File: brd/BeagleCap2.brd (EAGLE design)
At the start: 152.5 x 152 mm, 33 parts, among them IC2 7805TV, J2 DS18B20, J3 Battery, U1 DHT22, X1 Conn BNC : pH, X2 Conn BNC : Dissolved Oxygen, X3 Conn BNC : Conductivity, X4 Conn BNC : ORP

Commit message: Schematic updated with new PCB
Done by JayMcGee
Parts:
- LED1: device led:LED5MM -> led:SML0805
- R1, R10, R2, R3, R4, R5, R6, R7, R8, R9: device adafruit:0207/10 -> adafruit:R0805
- moved C2 96.6 mm to (-58.5, 76.5)
- moved J4 82.7 mm to (-6.50, 6.00)
- moved R8 76.2 mm to (-16.0, 6.00)
- moved D4 76.0 mm to (-16.0, 9.00)
- moved D3 75.7 mm to (-16.0, 0.50)
- moved R10 64.7 mm to (-16.0, 12.0)
- moved R9 64.0 mm to (-16.0, 3.00)
- moved LED1 61.1 mm to (-7.50, 81.5), turned to 0 degrees
- moved R7 56.0 mm to (-7.50, 79.0)
- moved C1 43.8 mm to (-52.0, 76.5)
- moved IC2 43.5 mm to (-29.1, 80.3)
- moved KK1 43.5 mm to (-29.0, 82.0)
- moved R2 16.0 mm to (-16.9, -6.34)
- moved R4 14.4 mm to (-28.6, -6.34)
- moved R1 14.1 mm to (-14.3, -6.84)
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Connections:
- net 3.3V renamed GNDX
- net N$2: now also LED1.C; no longer LED1.K
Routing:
- net GND: track 0.00 -> 36.8 mm
- net 5V: track 0.00 -> 35.8 mm
- net N$1: track 0.00 -> 15.6 mm
- net VIN: track 0.00 -> 8.85 mm
- added copper zone on layer 16, net GND
- added copper zone on layer 1, net GNDX
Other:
- board size 152.5 x 152 mm -> 75.5 x 152 mm
- board text added: "AQUARIUS"
- board text added: "Jean-Philippe Fournier Jean-Pascal McGee"
- board text removed: "SIM908"

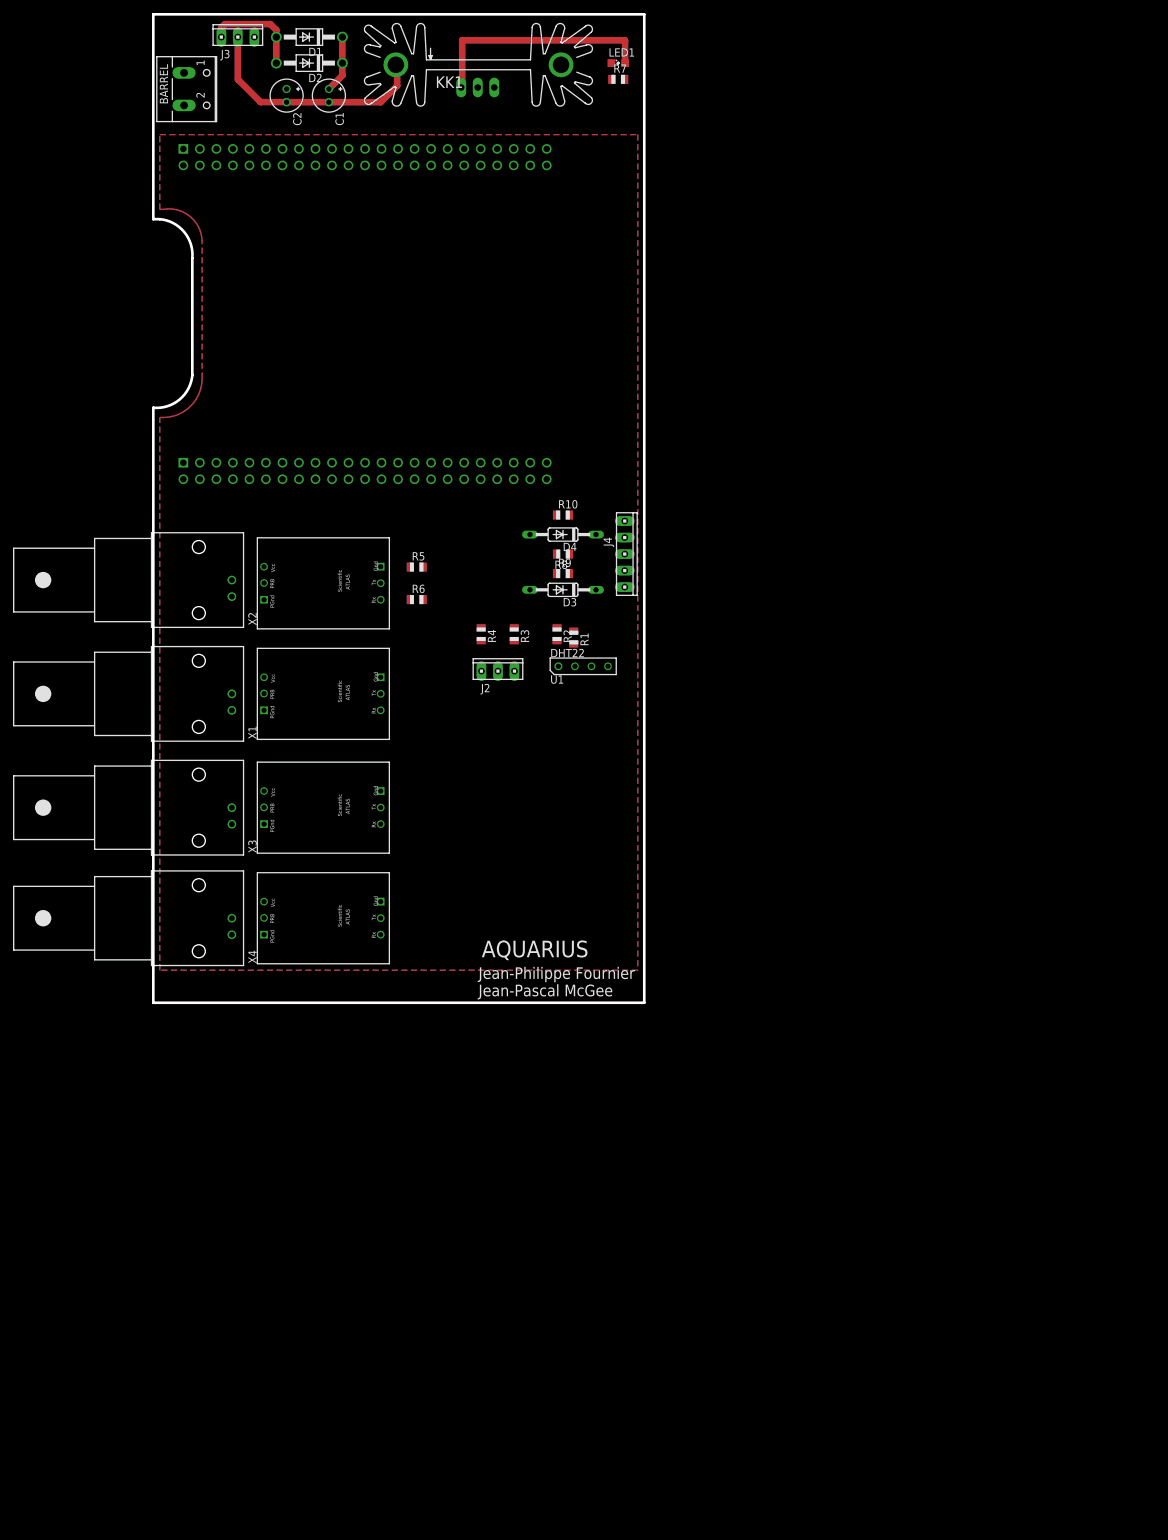
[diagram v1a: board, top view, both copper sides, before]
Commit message: Pcb updated, Fixed DRU error
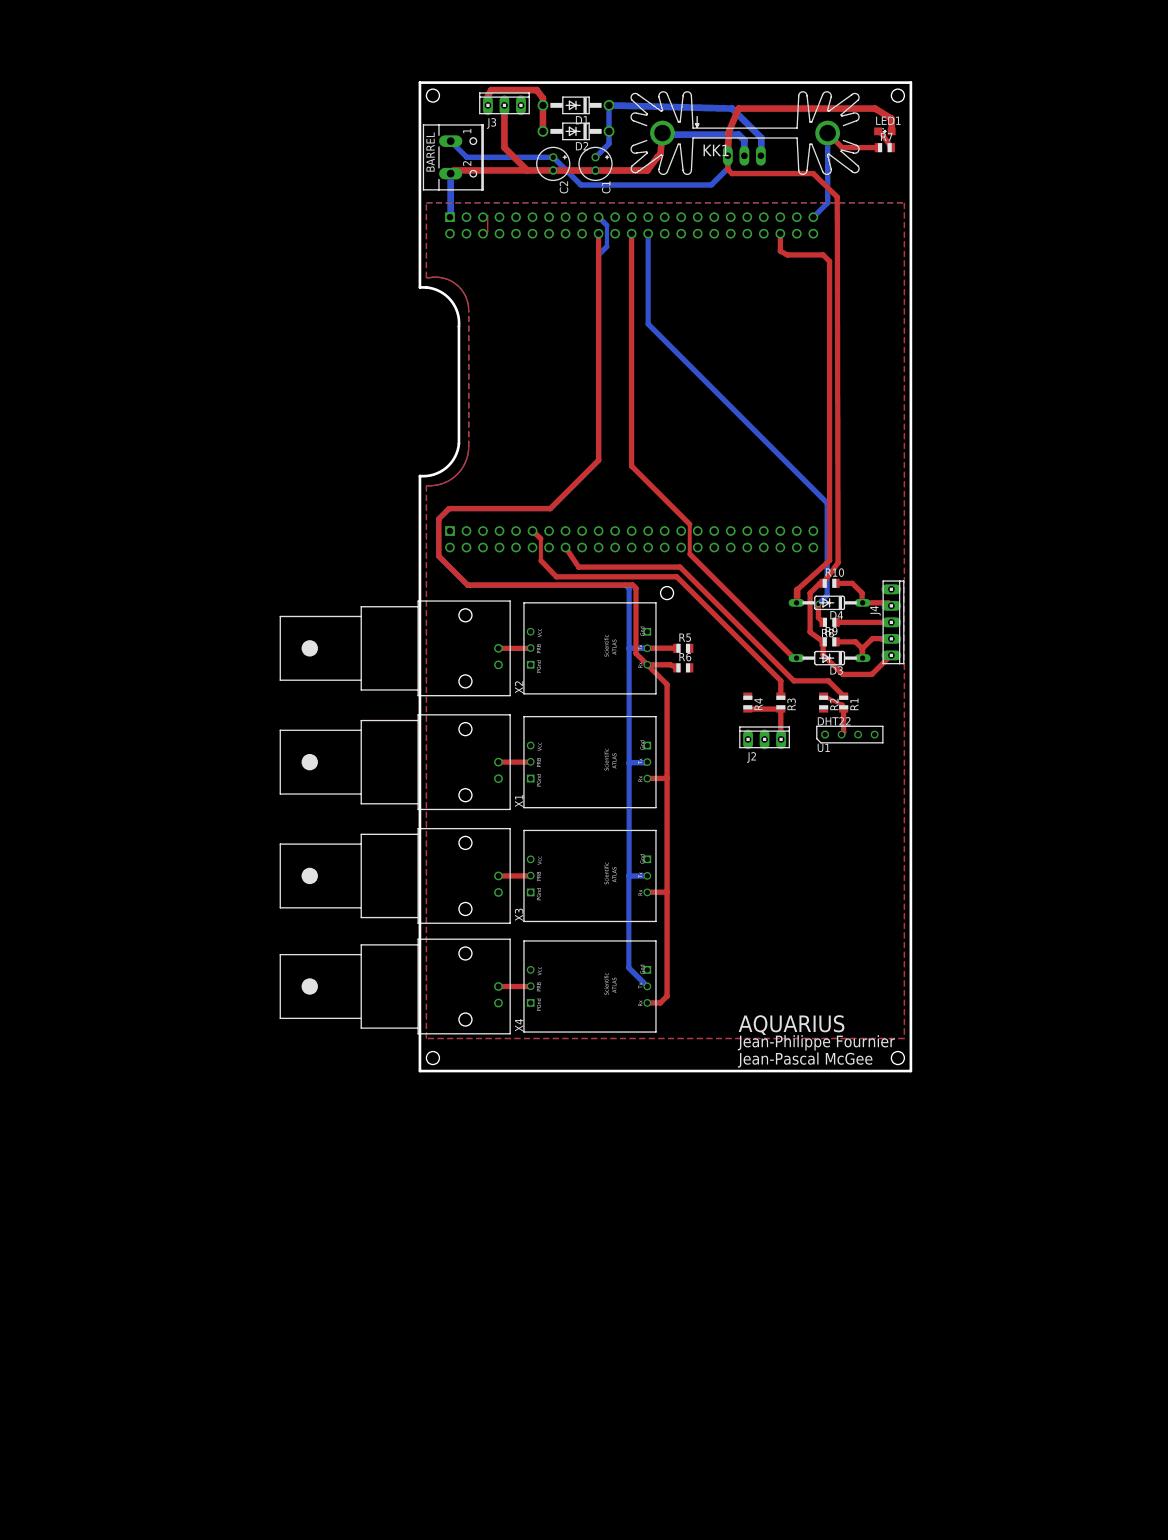
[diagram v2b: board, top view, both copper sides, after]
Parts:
- moved R5 42.9 mm to (2.50, -8.50)
- moved R1 42.7 mm to (27.2, -16.8)
- moved U$1 42.3 mm to (-52.4, 5.10)
- moved BARREL 42.3 mm to (-32.0, 67.0)
- moved C1 42.3 mm to (-11.0, 66.0)
- moved C2 42.3 mm to (-17.5, 66.0)
- moved D1 42.3 mm to (-14.0, 75.0)
- moved D2 42.3 mm to (-14.0, 71.0)
- moved D3 42.3 mm to (25.0, -10.0)
- moved D4 42.3 mm to (25.0, -1.50)
- moved IC2 42.3 mm to (11.9, 69.8)
- moved J2 42.3 mm to (15.0, -22.5)
- moved J3 42.3 mm to (-25.0, 75.0)
- moved J4 42.3 mm to (34.5, -4.50)
- moved KK1 42.3 mm to (12.0, 71.5)
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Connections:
- net GNDX renamed 3.3V
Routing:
- net I2C2_SDA: track 0.00 -> 180.1 mm
- net I2C2_SCL: track 0.00 -> 179.2 mm
- net 5V: track 35.8 -> 188.8 mm
- net TX: track 0.00 -> 76.0 mm
- net RX: track 0.00 -> 72.0 mm, vias 0 -> 1
- net P: track 0.00 -> 65.6 mm
- net GND: track 36.8 -> 93.1 mm
- net N$6: track 0.00 -> 52.6 mm
- net N$4: track 0.00 -> 52.0 mm
- net VIN: track 8.85 -> 36.9 mm
- net N$9: track 0.00 -> 12.5 mm
- net N$11: track 0.00 -> 10.8 mm
- net N$5: track 0.00 -> 9.78 mm
- net N$10: track 0.00 -> 8.50 mm
- net N$3: track 0.00 -> 7.91 mm
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
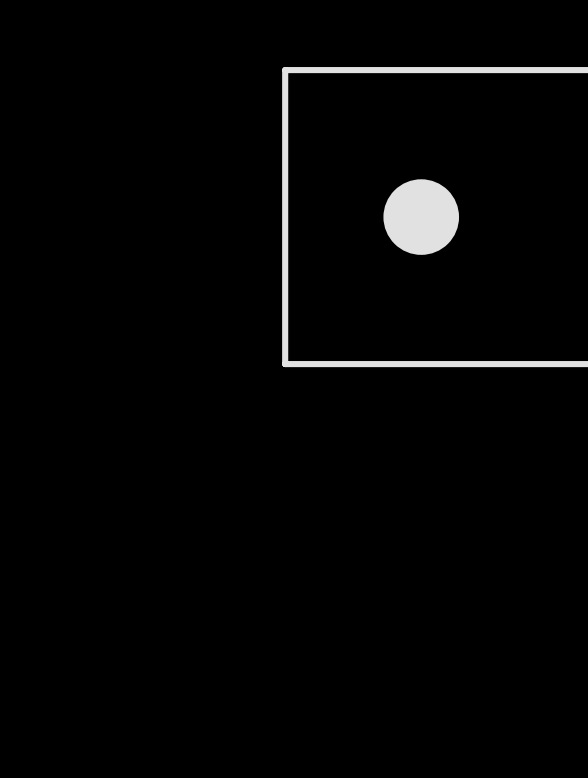
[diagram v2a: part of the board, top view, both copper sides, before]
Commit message: Added a switch to select mode of operation
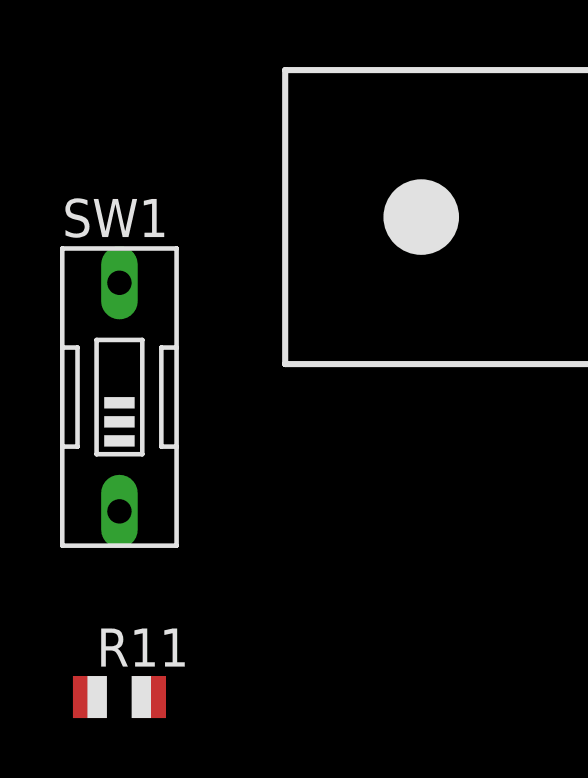
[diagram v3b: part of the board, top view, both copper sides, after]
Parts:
- added R11: 4.7K, adafruit:R0805
- added SW1: (no value), special:EDG-01
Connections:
- new net N$7: R11.1, SW1.2, U$1.58
- new net VCC: R11.2
- net GND: now also SW1.1
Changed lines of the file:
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@@
 <element name="C2" library="rcl" package="E2-5" value="10uF" x="-17.5" y="66" rot="R270"/>
 <element name="J4" library="con-amp" package="10X05MTA" value="" x="34.5" y="-4.5" rot="R270"/>
+<element name="SW1" library="special" package="EDG-01" value="" x="-65" y="-66.5"/>
+<element name="R11" library="adafruit" package="R0805" value="4.7K" x="-65" y="-76.5"/>
 </elements>
 <signals>
@@
 <wire x1="-33.27" y1="64.5" x2="-33.27" y2="57.915" width="1.016" layer="16"/>
 <wire x1="-33.27" y1="57.915" x2="-33.38" y2="57.805" width="1.016" layer="16"/>
+<contactref element="SW1" pad="1"/>
+<wire x1="-25.92" y1="-63.04" x2="-65" y2="-70.31" width="0" layer="19" extent="1-1"/>
+<wire x1="-20.97" y1="-63.025" x2="-25.92" y2="-63.04" width="0" layer="19" extent="1-1"/>
+<wire x1="-25.92" y1="-46.04" x2="-25.92" y2="-63.04" width="0" layer="19" extent="1-1"/>
+<wire x1="-20.97" y1="-46.025" x2="-25.92" y2="-46.04" width="0" layer="19" extent="1-1"/>
+<wire x1="-25.92" y1="-28.54" x2="-25.92" y2="-46.04" width="0" layer="19" extent="1-1"/>
+<wire x1="-20.97" y1="-28.525" x2="-25.92" y2="-28.54" width="0" layer="19" extent="1-1"/>
+<wire x1="-25.92" y1="-11.04" x2="-25.92" y2="-28.54" width="0" layer="19" extent="1-1"/>
+<wire x1="-20.97" y1="-11.025" x2="-25.92" y2="-11.04" width="0" layer="19" extent="1-1"/>
+<wire x1="-3.03" y1="-57.945" x2="-20.97" y2="-63.025" width="0" layer="19" extent="1-1"/>
+<wire x1="-3.03" y1="-40.945" x2="-3.03" y2="-57.945" width="0" layer="19" extent="1-1"/>
+<wire x1="-3.03" y1="-23.445" x2="-3.03" y2="-40.945" width="0" layer="19" extent="1-1"/>
+<wire x1="-3.03" y1="-5.945" x2="-3.03" y2="-23.445" width="0" layer="19" extent="1-1"/>
+<wire x1="15" y1="-22.5" x2="-3.03" y2="-23.445" width="0" layer="19" extent="1-1"/>
+<wire x1="31.92" y1="-21.76" x2="15" y2="-22.5" width="0" layer="19" extent="1-1"/>
+<wire x1="-33.38" y1="7.005" x2="-25.92" y2="-11.04" width="0" layer="19" extent="1-1"/>
+<wire x1="-33.38" y1="9.545" x2="-33.38" y2="7.005" width="0" layer="19" extent="1-1"/>
+<wire x1="34.5" y1="0.58" x2="31.92" y2="-21.76" width="0" layer="19" extent="1-1"/>
+<wire x1="-33.38" y1="55.265" x2="-33.38" y2="9.545" width="0" layer="19" extent="1-1"/>
+<wire x1="-33.38" y1="57.805" x2="-33.38" y2="55.265" width="0" layer="19" extent="1-1"/>
+<wire x1="19.96" y1="57.805" x2="11.89" y2="67.25" width="0" layer="19" extent="1-1"/>
+<wire x1="22.5" y1="57.805" x2="19.96" y2="57.805" width="0" layer="19" extent="1-1"/>
+<wire x1="22.5" y1="55.265" x2="22.5" y2="57.805" width="0" layer="19" extent="1-1"/>
+<wire x1="19.96" y1="55.265" x2="19.96" y2="57.805" width="0" layer="19" extent="1-1"/>
 </signal>
 <signal name="VIN">
@@
 <wire x1="9.35" y1="65.3" x2="9.35" y2="67.25" width="0.8128" layer="16"/>
 </signal>
+<signal name="N$7">
+<contactref element="U$1" pad="58"/>
+<contactref element="SW1" pad="2"/>
+<contactref element="R11" pad="1"/>
+<wire x1="-65" y1="-62.69" x2="-66" y2="-76.5" width="0" layer="19" extent="1-1"/>
+<wire x1="-20.68" y1="55.265" x2="-65" y2="-62.69" width="0" layer="19" extent="1-1"/>
+</signal>
+<signal name="VCC">
+<contactref element="R11" pad="2"/>
+</signal>
 </signals>
